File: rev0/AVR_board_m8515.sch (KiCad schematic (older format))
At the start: 15 parts

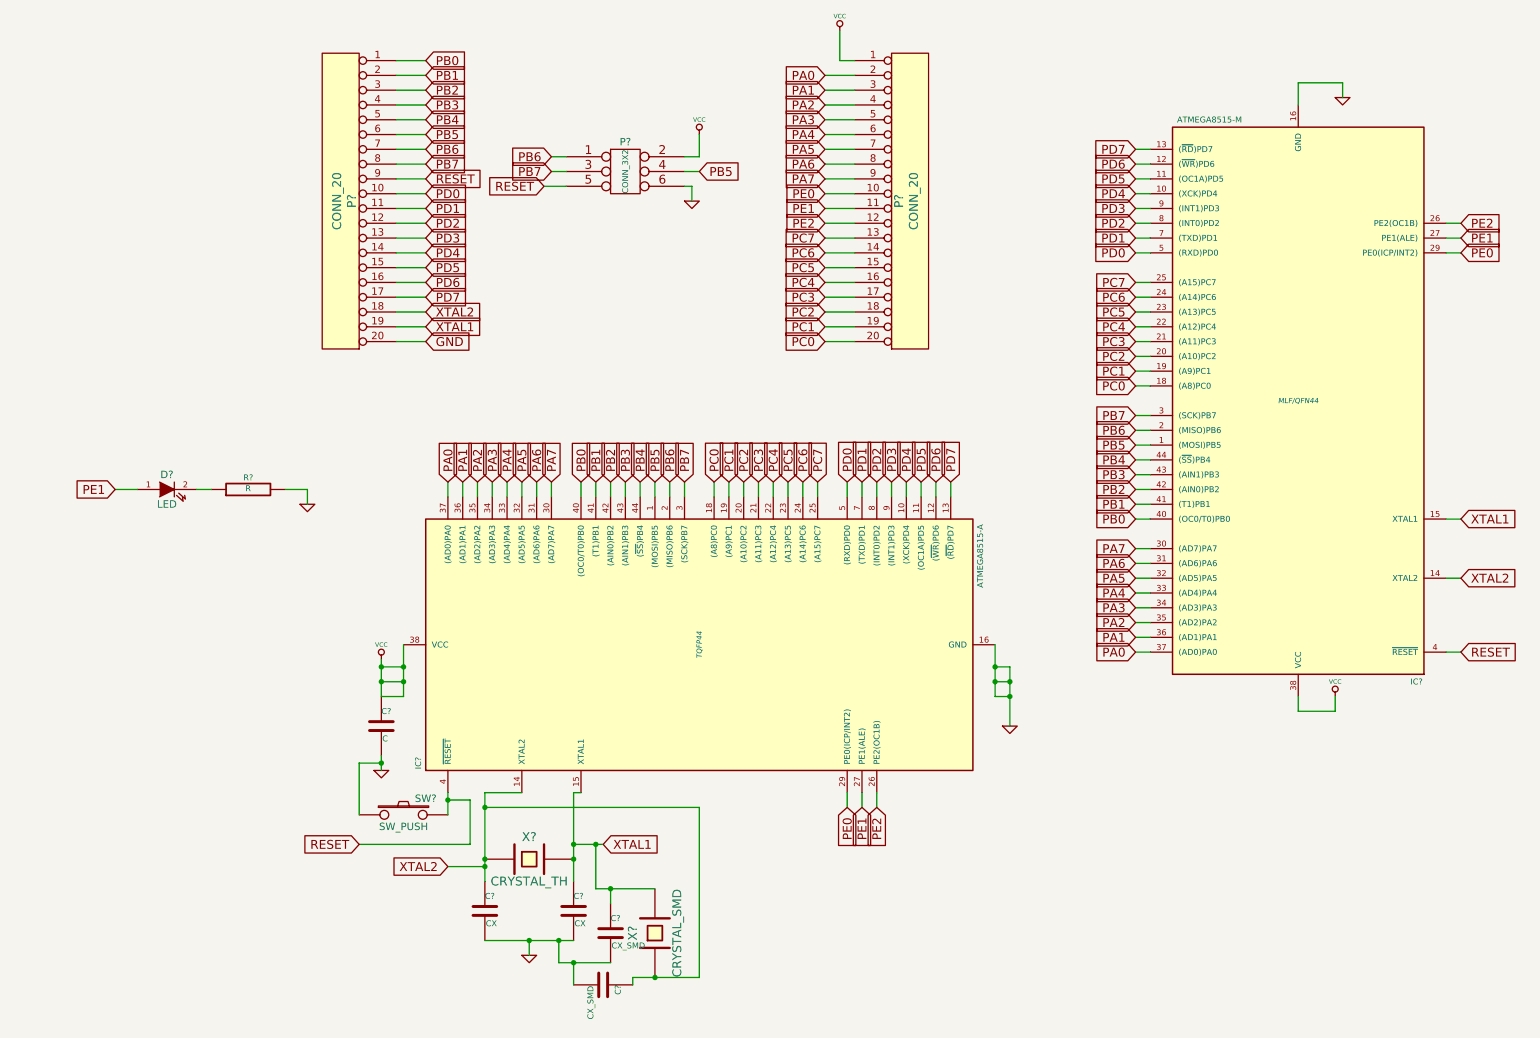
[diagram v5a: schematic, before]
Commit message: made netlist, connected to most footprints
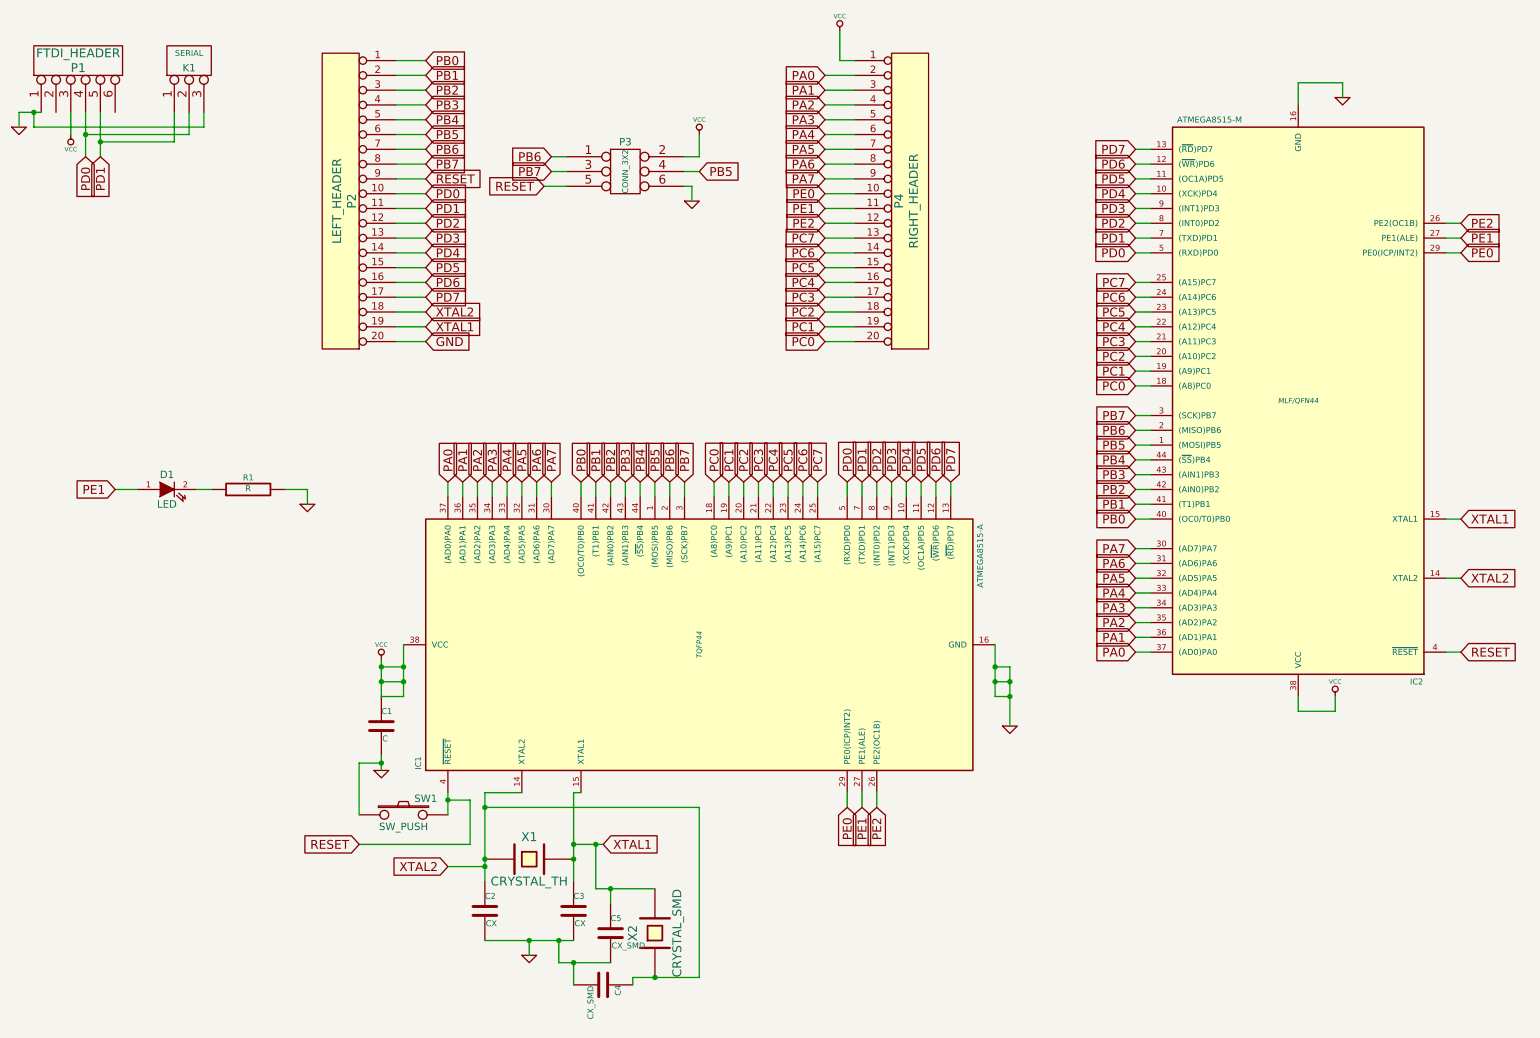
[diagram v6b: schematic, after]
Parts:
- added K1: SERIAL, symbol CONN_3
- added P1: FTDI_HEADER, symbol CONN_6
- P2: renamed from P?; value CONN_20 -> LEFT_HEADER
- P4: renamed from P?; value CONN_20 -> RIGHT_HEADER
- gave numbers to parts that had none: 13
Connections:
- net GND: now also K1.3 (P3), P1.1
- net PD0: now also K1.2 (PM), P1.4
- net PD1: now also K1.1 (P1), P1.5
- net VCC: now also P1.3
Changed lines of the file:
@@
 $EndDescr
 $Comp
-L CRYSTAL X?
+L CRYSTAL X1
 U 1 1 54186AE5
 P 4500 6400
-F 0 "X?" H 4500 6550 60  0000 C CNN
+F 0 "X1" H 4500 6550 60  0000 C CNN
 F 1 "CRYSTAL_TH" H 4500 6250 60  0000 C CNN
 F 2 "" H 4500 6400 60  0000 C CNN
@@
 $EndComp
 $Comp
-L C C?
+L C C3
 U 1 1 54186B33
 P 4800 6750
-F 0 "C?" H 4800 6850 40  0000 L CNN
+F 0 "C3" H 4800 6850 40  0000 L CNN
 F 1 "CX" H 4806 6665 40  0000 L CNN
 F 2 "" H 4838 6600 30  0000 C CNN
@@
 $EndComp
 $Comp
-L C C?
+L C C2
 U 1 1 54186B4B
 P 4200 6750
-F 0 "C?" H 4200 6850 40  0000 L CNN
+F 0 "C2" H 4200 6850 40  0000 L CNN
 F 1 "CX" H 4206 6665 40  0000 L CNN
 F 2 "" H 4238 6600 30  0000 C CNN
@@
 $EndComp
 $Comp
-L GND #PWR?
+L GND #PWR6
 U 1 1 54186B5E
 P 4500 7050
-F 0 "#PWR?" H 4500 7050 30  0001 C CNN
+F 0 "#PWR6" H 4500 7050 30  0001 C CNN
 F 1 "GND" H 4500 6980 30  0001 C CNN
 F 2 "" H 4500 7050 60  0000 C CNN
@@
 Connection ~ 4200 6400
 $Comp
-L C C?
+L C C1
 U 1 1 54186C0A
 P 3500 5500
-F 0 "C?" H 3500 5600 40  0000 L CNN
+F 0 "C1" H 3500 5600 40  0000 L CNN
 F 1 "C" H 3506 5415 40  0000 L CNN
 F 2 "" H 3538 5350 30  0000 C CNN
@@
 $EndComp
 $Comp
-L GND #PWR?
+L GND #PWR5
 U 1 1 54186C19
 P 3500 5800
-F 0 "#PWR?" H 3500 5800 30  0001 C CNN
+F 0 "#PWR5" H 3500 5800 30  0001 C CNN
 F 1 "GND" H 3500 5730 30  0001 C CNN
 F 2 "" H 3500 5800 60  0000 C CNN
@@
 $EndComp
 $Comp
-L VCC #PWR?
+L VCC #PWR4
 U 1 1 54186C37
 P 3500 5050
-F 0 "#PWR?" H 3500 5150 30  0001 C CNN
+F 0 "#PWR4" H 3500 5150 30  0001 C CNN
 F 1 "VCC" H 3500 5150 30  0000 C CNN
 F 2 "" H 3500 5050 60  0000 C CNN
@@
 	3500 5300 3650 5300
 $Comp
-L GND #PWR?
+L GND #PWR10
 U 1 1 54186C8C
 P 7750 5500
-F 0 "#PWR?" H 7750 5500 30  0001 C CNN
+F 0 "#PWR10" H 7750 5500 30  0001 C CNN
 F 1 "GND" H 7750 5430 30  0001 C CNN
 F 2 "" H 7750 5500 60  0000 C CNN
@@
 Connection ~ 7750 5300
 $Comp
-L SW_PUSH SW?
+L SW_PUSH SW1
 U 1 1 54186D3B
 P 3650 6100
-F 0 "SW?" H 3800 6210 50  0000 C CNN
+F 0 "SW1" H 3800 6210 50  0000 C CNN
 F 1 "SW_PUSH" H 3650 6020 50  0000 C CNN
 F 2 "" H 3650 6100 60  0000 C CNN
@@
 Connection ~ 3500 5750
 $Comp
-L CONN_20 P?
+L CONN_20 P4
 U 1 1 54186E86
 P 7050 1950
-F 0 "P?" V 7000 1950 60  0000 C CNN
-F 1 "CONN_20" V 7100 1950 60  0000 C CNN
+F 0 "P4" V 7000 1950 60  0000 C CNN
+F 1 "RIGHT_HEADER" V 7100 1950 60  0000 C CNN
 F 2 "" H 7050 1950 60  0000 C CNN
 F 3 "" H 7050 1950 60  0000 C CNN
@@
 $EndComp
 $Comp
-L CONN_20 P?
+L CONN_20 P2
 U 1 1 54186E9A
 P 3250 1950
-F 0 "P?" V 3200 1950 60  0000 C CNN
-F 1 "CONN_20" V 3300 1950 60  0000 C CNN
+F 0 "P2" V 3200 1950 60  0000 C CNN
+F 1 "LEFT_HEADER" V 3300 1950 60  0000 C CNN
 F 2 "" H 3250 1950 60  0000 C CNN
 F 3 "" H 3250 1950 60  0000 C CNN
@@
 PC7
 $Comp
-L ATMEGA8515-A IC?
+L ATMEGA8515-A IC1
 U 1 1 54187500
 P 5650 4950
-F 0 "IC?" H 4850 6850 40  0000 C CNN
+F 0 "IC1" H 4850 6850 40  0000 C CNN
 F 1 "ATMEGA8515-A" H 6250 3050 40  0000 C CNN
 F 2 "TQFP44" H 5650 4950 35  0000 C CIN
@@
 	7350 3850 7350 3950
 $Comp
-L VCC #PWR?
+L VCC #PWR9
 U 1 1 54189251
 P 6600 800
-F 0 "#PWR?" H 6600 900 30  0001 C CNN
+F 0 "#PWR9" H 6600 900 30  0001 C CNN
 F 1 "VCC" H 6600 900 30  0000 C CNN
 F 2 "" H 6600 800 60  0000 C CNN
@@
 	6500 2900 6700 2900
 $Comp
-L ATMEGA8515-M IC?
+L ATMEGA8515-M IC2
 U 1 1 5418A671
 P 9700 3300
-F 0 "IC?" H 8900 5200 40  0000 C CNN
+F 0 "IC2" H 8900 5200 40  0000 C CNN
 F 1 "ATMEGA8515-M" H 10300 1400 40  0000 C CNN
 F 2 "MLF/QFN44" H 9700 3300 35  0000 C CIN
@@
 $EndComp
 $Comp
-L GND #PWR?
+L GND #PWR12
 U 1 1 5418A680
 P 10000 1250
-F 0 "#PWR?" H 10000 1250 30  0001 C CNN
+F 0 "#PWR12" H 10000 1250 30  0001 C CNN
 F 1 "GND" H 10000 1180 30  0001 C CNN
 F 2 "" H 10000 1250 60  0000 C CNN
@@
 PA0
 $Comp
-L VCC #PWR?
+L VCC #PWR11
 U 1 1 5418A7C7
 P 9950 5300
-F 0 "#PWR?" H 9950 5400 30  0001 C CNN
+F 0 "#PWR11" H 9950 5400 30  0001 C CNN
 F 1 "VCC" H 9950 5400 30  0000 C CNN
 F 2 "" H 9950 5300 60  0000 C CNN
@@
 	8700 5000 8600 5000
 $Comp
-L CONN_3X2 P?
+L CONN_3X2 P3
 U 1 1 5418C01F
 P 5150 1800
-F 0 "P?" H 5150 2050 50  0000 C CNN
+F 0 "P3" H 5150 2050 50  0000 C CNN
 F 1 "CONN_3X2" V 5150 1850 40  0000 C CNN
 F 2 "" H 5150 1800 60  0000 C CNN
@@
 $EndComp
 $Comp
-L VCC #PWR?
+L VCC #PWR8
 U 1 1 5418C02E
 P 5650 1500
-F 0 "#PWR?" H 5650 1600 30  0001 C CNN
+F 0 "#PWR8" H 5650 1600 30  0001 C CNN
 F 1 "VCC" H 5650 1600 30  0000 C CNN
 F 2 "" H 5650 1500 60  0000 C CNN
@@
 PB5
 $Comp
-L GND #PWR?
+L GND #PWR7
 U 1 1 5418C0DE
 P 5600 1950
-F 0 "#PWR?" H 5600 1950 30  0001 C CNN
+F 0 "#PWR7" H 5600 1950 30  0001 C CNN
 F 1 "GND" H 5600 1880 30  0001 C CNN
 F 2 "" H 5600 1950 60  0000 C CNN
@@
 	4750 1850 4600 1850
 $Comp
-L CRYSTAL X?
+L CRYSTAL X2
 U 1 1 5418E675
 P 5350 6900
-F 0 "X?" H 5350 7050 60  0000 C CNN
+F 0 "X2" H 5350 7050 60  0000 C CNN
 F 1 "CRYSTAL_SMD" H 5350 6750 60  0000 C CNN
 F 2 "" H 5350 6900 60  0000 C CNN
@@
 Connection ~ 4200 6050
 $Comp
-L C C?
+L C C5
 U 1 1 5418E983
 P 5050 6900
-F 0 "C?" H 5050 7000 40  0000 L CNN
+F 0 "C5" H 5050 7000 40  0000 L CNN
 F 1 "CX_SMD" H 5056 6815 40  0000 L CNN
 F 2 "" H 5088 6750 30  0000 C CNN
@@
 Connection ~ 4700 6950
 $Comp
-L C C?
+L C C4
 U 1 1 5418EAF3
 P 5000 7250
-F 0 "C?" H 5000 7350 40  0000 L CNN
+F 0 "C4" H 5000 7350 40  0000 L CNN
 F 1 "CX_SMD" H 5006 7165 40  0000 L CNN
 F 2 "" H 5038 7100 30  0000 C CNN
@@
 Connection ~ 4800 7100
 $Comp
-L LED D?
+L LED D1
 U 1 1 5418EEE7
 P 2050 3900
-F 0 "D?" H 2050 4000 50  0000 C CNN
+F 0 "D1" H 2050 4000 50  0000 C CNN
 F 1 "LED" H 2050 3800 50  0000 C CNN
 F 2 "" H 2050 3900 60  0000 C CNN
@@
 PE1
 $Comp
-L R R?
+L R R1
 U 1 1 5418EEF6
 P 2600 3900
-F 0 "R?" V 2680 3900 40  0000 C CNN
+F 0 "R1" V 2680 3900 40  0000 C CNN
 F 1 "R" V 2607 3901 40  0000 C CNN
 F 2 "" V 2530 3900 30  0000 C CNN
@@
 	2250 3900 2350 3900
 $Comp
-L GND #PWR?
+L GND #PWR3
 U 1 1 5418F076
 P 3000 4000
-F 0 "#PWR?" H 3000 4000 30  0001 C CNN
+F 0 "#PWR3" H 3000 4000 30  0001 C CNN
 F 1 "GND" H 3000 3930 30  0001 C CNN
 F 2 "" H 3000 4000 60  0000 C CNN
@@
 Wire Wire Line
 	3000 3900 3000 4000
+$Comp
+L CONN_6 P1
+U 1 1 5418F4ED
+P 1450 1000
+F 0 "P1" V 1400 1000 60  0000 C CNN
+F 1 "FTDI_HEADER" V 1500 1000 60  0000 C CNN
+F 2 "" H 1450 1000 60  0000 C CNN
+F 3 "" H 1450 1000 60  0000 C CNN
+	1    1450 1000
+	0    -1   -1   0
+$EndComp
+$Comp
+L GND #PWR1
+U 1 1 5418F501
+P 1050 1450
+F 0 "#PWR1" H 1050 1450 30  0001 C CNN
+F 1 "GND" H 1050 1380 30  0001 C CNN
+F 2 "" H 1050 1450 60  0000 C CNN
+F 3 "" H 1050 1450 60  0000 C CNN
+	1    1050 1450
+	1    0    0    -1
+$EndComp
+Wire Wire Line
+	1200 1350 1050 1350
+Wire Wire Line
+	1050 1350 1050 1450
+$Comp
+L VCC #PWR2
+U 1 1 5418F6CA
+P 1400 1500
+F 0 "#PWR2" H 1400 1600 30  0001 C CNN
+F 1 "VCC" H 1400 1600 30  0000 C CNN
+F 2 "" H 1400 1500 60  0000 C CNN
+F 3 "" H 1400 1500 60  0000 C CNN
+	1    1400 1500
+	-1   0    0    1
+$EndComp
+Wire Wire Line
+	1400 1350 1400 1500
+Text GLabel 1500 1650 3    60   Input ~ 0
+PD0
+Wire Wire Line
+	1500 1350 1500 1650
+Text GLabel 1600 1650 3    60   Input ~ 0
+PD1
+Wire Wire Line
+	1600 1350 1600 1650
+$Comp
+L CONN_3 K1
+U 1 1 5418FA1D
+P 2200 1000
+F 0 "K1" V 2150 1000 50  0000 C CNN
+F 1 "SERIAL" V 2250 1000 40  0000 C CNN
+F 2 "" H 2200 1000 60  0000 C CNN
+F 3 "" H 2200 1000 60  0000 C CNN
+	1    2200 1000
+	0    -1   -1   0
+$EndComp
+Wire Wire Line
+	2100 1350 2100 1550
+Wire Wire Line
+	2100 1550 1600 1550
+Connection ~ 1600 1550
+Wire Wire Line
+	2200 1350 2200 1500
+Wire Wire Line
+	2200 1500 1500 1500
+Connection ~ 1500 1500
+Wire Wire Line
+	2300 1350 2300 1450
+Wire Wire Line
+	2300 1450 1150 1450
+Wire Wire Line
+	1150 1450 1150 1350
+Connection ~ 1150 1350
 $EndSCHEMATC

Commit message: added logo mod file, also added silkscreen refs
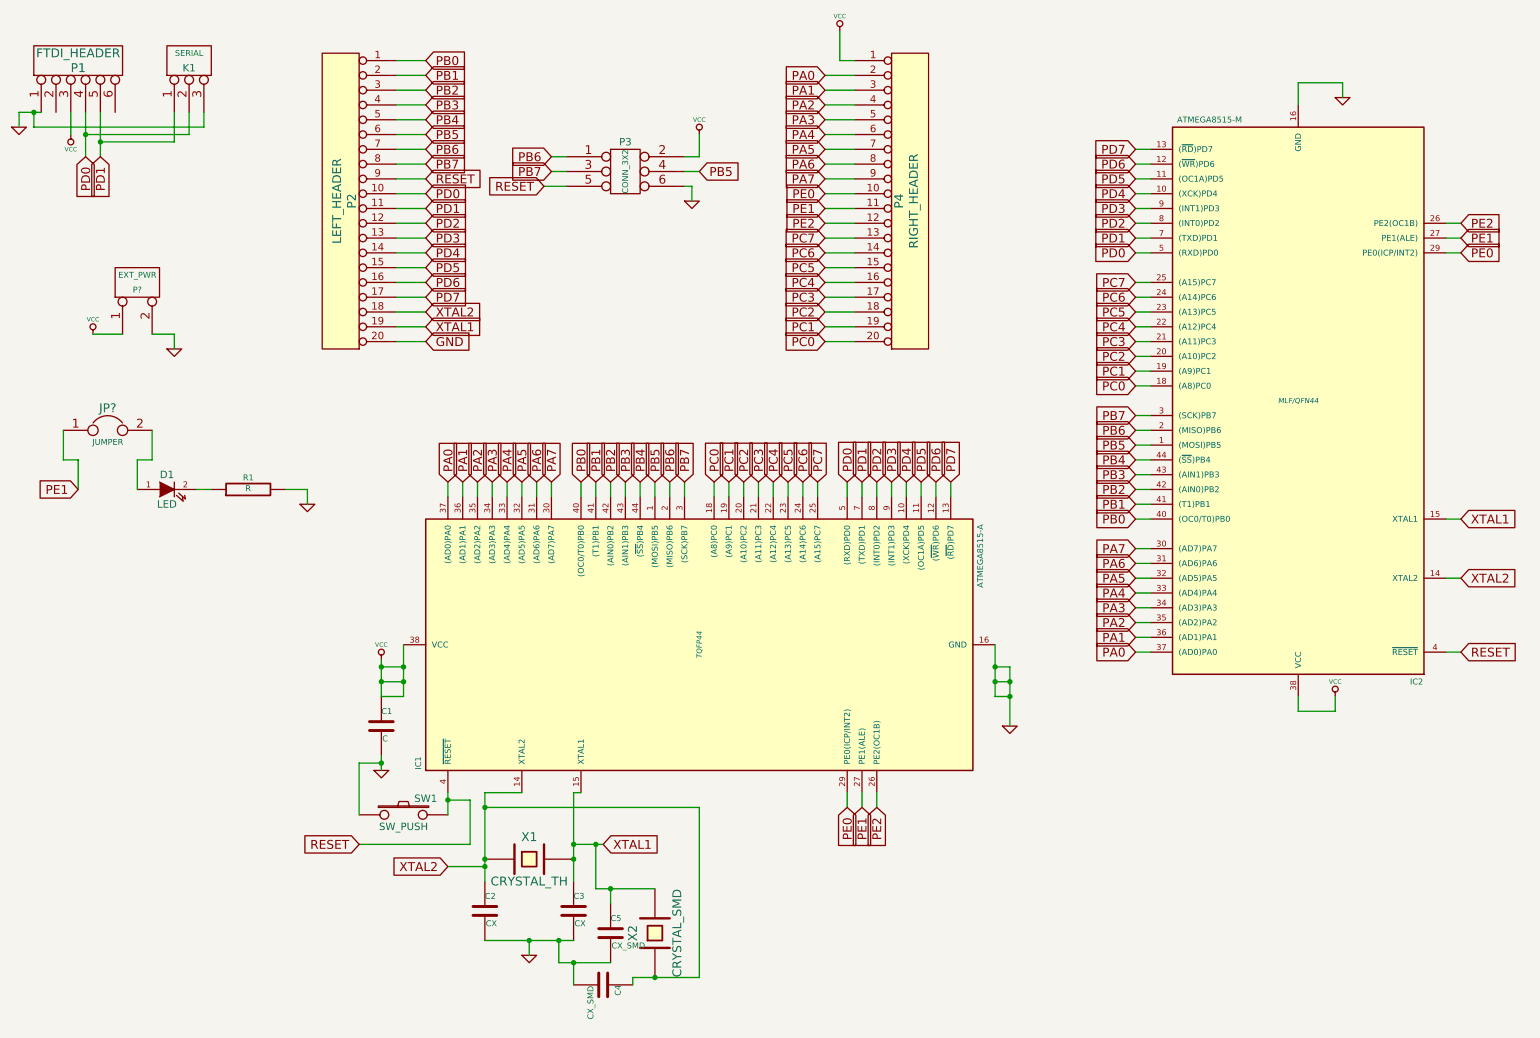
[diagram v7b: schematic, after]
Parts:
- added JP?: JUMPER, symbol JUMPER
- added P?: EXT_PWR, symbol CONN_2
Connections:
- net GND: now also P?.2 (PM)
- net PE1: now also JP?.1; no longer D1.1 (A)
- net VCC: now also P?.1 (P1)
- new net: D1.1 (A), JP?.2
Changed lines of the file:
@@
 $EndComp
 $Comp
-L GND #PWR6
+L GND #PWR01
 U 1 1 54186B5E
 P 4500 7050
-F 0 "#PWR6" H 4500 7050 30  0001 C CNN
+F 0 "#PWR01" H 4500 7050 30  0001 C CNN
 F 1 "GND" H 4500 6980 30  0001 C CNN
 F 2 "" H 4500 7050 60  0000 C CNN
@@
 $EndComp
 $Comp
-L GND #PWR5
+L GND #PWR02
 U 1 1 54186C19
 P 3500 5800
-F 0 "#PWR5" H 3500 5800 30  0001 C CNN
+F 0 "#PWR02" H 3500 5800 30  0001 C CNN
 F 1 "GND" H 3500 5730 30  0001 C CNN
 F 2 "" H 3500 5800 60  0000 C CNN
@@
 $EndComp
 $Comp
-L VCC #PWR4
+L VCC #PWR03
 U 1 1 54186C37
 P 3500 5050
-F 0 "#PWR4" H 3500 5150 30  0001 C CNN
+F 0 "#PWR03" H 3500 5150 30  0001 C CNN
 F 1 "VCC" H 3500 5150 30  0000 C CNN
 F 2 "" H 3500 5050 60  0000 C CNN
@@
 	3500 5300 3650 5300
 $Comp
-L GND #PWR10
+L GND #PWR04
 U 1 1 54186C8C
 P 7750 5500
-F 0 "#PWR10" H 7750 5500 30  0001 C CNN
+F 0 "#PWR04" H 7750 5500 30  0001 C CNN
 F 1 "GND" H 7750 5430 30  0001 C CNN
 F 2 "" H 7750 5500 60  0000 C CNN
@@
 	7350 3850 7350 3950
 $Comp
-L VCC #PWR9
+L VCC #PWR05
 U 1 1 54189251
 P 6600 800
-F 0 "#PWR9" H 6600 900 30  0001 C CNN
+F 0 "#PWR05" H 6600 900 30  0001 C CNN
 F 1 "VCC" H 6600 900 30  0000 C CNN
 F 2 "" H 6600 800 60  0000 C CNN
@@
 $EndComp
 $Comp
-L GND #PWR12
+L GND #PWR06
 U 1 1 5418A680
 P 10000 1250
-F 0 "#PWR12" H 10000 1250 30  0001 C CNN
+F 0 "#PWR06" H 10000 1250 30  0001 C CNN
 F 1 "GND" H 10000 1180 30  0001 C CNN
 F 2 "" H 10000 1250 60  0000 C CNN
@@
 PA0
 $Comp
-L VCC #PWR11
+L VCC #PWR07
 U 1 1 5418A7C7
 P 9950 5300
-F 0 "#PWR11" H 9950 5400 30  0001 C CNN
+F 0 "#PWR07" H 9950 5400 30  0001 C CNN
 F 1 "VCC" H 9950 5400 30  0000 C CNN
 F 2 "" H 9950 5300 60  0000 C CNN
@@
 $EndComp
 $Comp
-L VCC #PWR8
+L VCC #PWR08
 U 1 1 5418C02E
 P 5650 1500
-F 0 "#PWR8" H 5650 1600 30  0001 C CNN
+F 0 "#PWR08" H 5650 1600 30  0001 C CNN
 F 1 "VCC" H 5650 1600 30  0000 C CNN
 F 2 "" H 5650 1500 60  0000 C CNN
@@
 PB5
 $Comp
-L GND #PWR7
+L GND #PWR09
 U 1 1 5418C0DE
 P 5600 1950
-F 0 "#PWR7" H 5600 1950 30  0001 C CNN
+F 0 "#PWR09" H 5600 1950 30  0001 C CNN
 F 1 "GND" H 5600 1880 30  0001 C CNN
 F 2 "" H 5600 1950 60  0000 C CNN
@@
 $EndComp
 Wire Wire Line
-	5350 6600 4950 6600
+	4950 6600 5350 6600
 Wire Wire Line
 	4950 6600 4950 6300
@@
 Connection ~ 5050 6600
 Wire Wire Line
-	5050 7100 4700 7100
+	4700 7100 5050 7100
 Wire Wire Line
 	4700 7100 4700 6950
@@
 	1    0    0    -1
 $EndComp
-Text GLabel 1700 3900 0    60   Input ~ 0
+Text GLabel 1450 3900 0    60   Input ~ 0
 PE1
 $Comp
@@
 $EndComp
 Wire Wire Line
-	1700 3900 1850 3900
-Wire Wire Line
 	2250 3900 2350 3900
 $Comp
-L GND #PWR3
+L GND #PWR010
 U 1 1 5418F076
 P 3000 4000
-F 0 "#PWR3" H 3000 4000 30  0001 C CNN
+F 0 "#PWR010" H 3000 4000 30  0001 C CNN
 F 1 "GND" H 3000 3930 30  0001 C CNN
 F 2 "" H 3000 4000 60  0000 C CNN
@@
 $EndComp
 $Comp
-L GND #PWR1
+L GND #PWR011
 U 1 1 5418F501
 P 1050 1450
-F 0 "#PWR1" H 1050 1450 30  0001 C CNN
+F 0 "#PWR011" H 1050 1450 30  0001 C CNN
 F 1 "GND" H 1050 1380 30  0001 C CNN
 F 2 "" H 1050 1450 60  0000 C CNN
@@
 $EndComp
 Wire Wire Line
-	1200 1350 1050 1350
+	1050 1350 1200 1350
 Wire Wire Line
 	1050 1350 1050 1450
 $Comp
-L VCC #PWR2
+L VCC #PWR012
 U 1 1 5418F6CA
 P 1400 1500
-F 0 "#PWR2" H 1400 1600 30  0001 C CNN
+F 0 "#PWR012" H 1400 1600 30  0001 C CNN
 F 1 "VCC" H 1400 1600 30  0000 C CNN
 F 2 "" H 1400 1500 60  0000 C CNN
@@
 	1150 1450 1150 1350
 Connection ~ 1150 1350
+$Comp
+L CONN_2 P?
+U 1 1 54190E9B
+P 1850 2500
+F 0 "P?" V 1800 2500 40  0000 C CNN
+F 1 "EXT_PWR" V 1900 2500 40  0000 C CNN
+F 2 "" H 1850 2500 60  0000 C CNN
+F 3 "" H 1850 2500 60  0000 C CNN
+	1    1850 2500
+	0    -1   -1   0
+$EndComp
+$Comp
+L VCC #PWR?
+U 1 1 54190EB4
+P 1550 2850
+F 0 "#PWR?" H 1550 2950 30  0001 C CNN
+F 1 "VCC" H 1550 2950 30  0000 C CNN
+F 2 "" H 1550 2850 60  0000 C CNN
+F 3 "" H 1550 2850 60  0000 C CNN
+	1    1550 2850
+	1    0    0    -1
+$EndComp
+$Comp
+L GND #PWR?
+U 1 1 54190EC3
+P 2100 2950
+F 0 "#PWR?" H 2100 2950 30  0001 C CNN
+F 1 "GND" H 2100 2880 30  0001 C CNN
+F 2 "" H 2100 2950 60  0000 C CNN
+F 3 "" H 2100 2950 60  0000 C CNN
+	1    2100 2950
+	1    0    0    -1
+$EndComp
+Wire Wire Line
+	1950 2850 2100 2850
+Wire Wire Line
+	2100 2850 2100 2950
+Wire Wire Line
+	1750 2850 1550 2850
+$Comp
+L JUMPER JP?
+U 1 1 54191199
+P 1650 3500
+F 0 "JP?" H 1650 3650 60  0000 C CNN
+F 1 "JUMPER" H 1650 3420 40  0000 C CNN
+F 2 "" H 1650 3500 60  0000 C CNN
+F 3 "" H 1650 3500 60  0000 C CNN
+	1    1650 3500
+	1    0    0    -1
+$EndComp
+Wire Wire Line
+	1950 3500 1950 3700
+Wire Wire Line
+	1950 3700 1850 3700
+Wire Wire Line
+	1850 3700 1850 3900
+Wire Wire Line
+	1350 3500 1350 3700
+Wire Wire Line
+	1350 3700 1450 3700
+Wire Wire Line
+	1450 3700 1450 3900
 $EndSCHEMATC
